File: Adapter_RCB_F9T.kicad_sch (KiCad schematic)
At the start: 48 parts, among them J1 USB_B_Micro, J2 Conn_01x04, J41 RCB_F9T, J51 Conn_Coaxial, J61 Conn_Coaxial, U11 XC6206PxxxMR, U21 LM27761, U31 CP2102-GMR-xQFN28, U51 BUF602xDBV, U61 BUF602xDBV

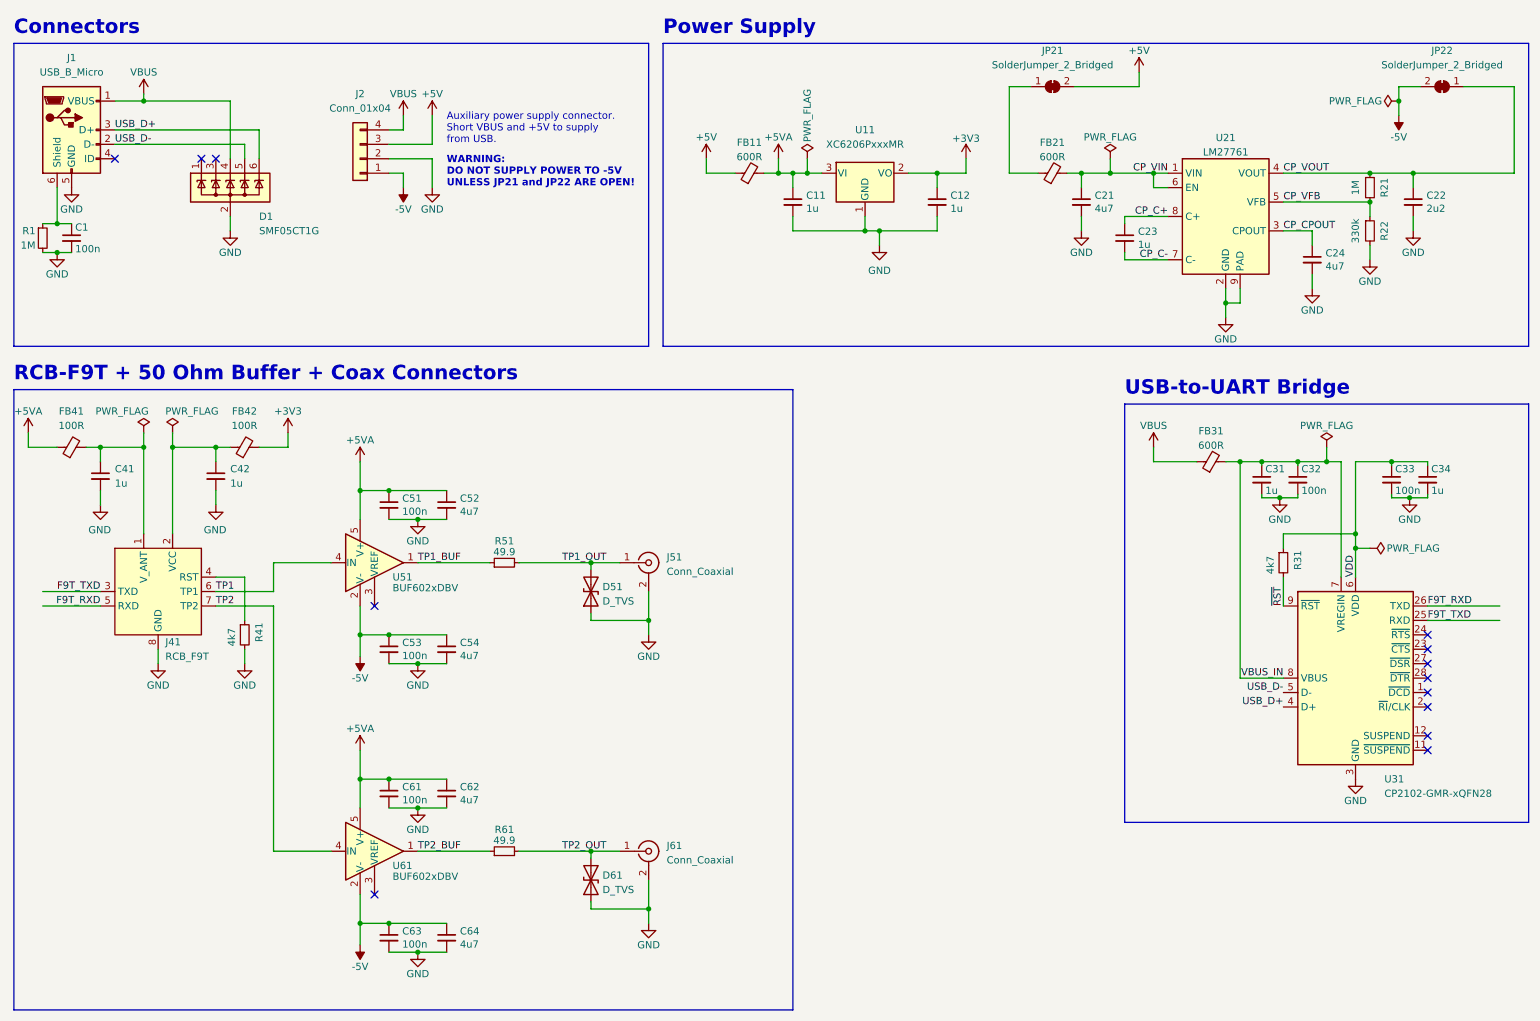
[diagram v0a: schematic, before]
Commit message: fix RCB-F9T NRST issue and move FB41 further away from mounting hole
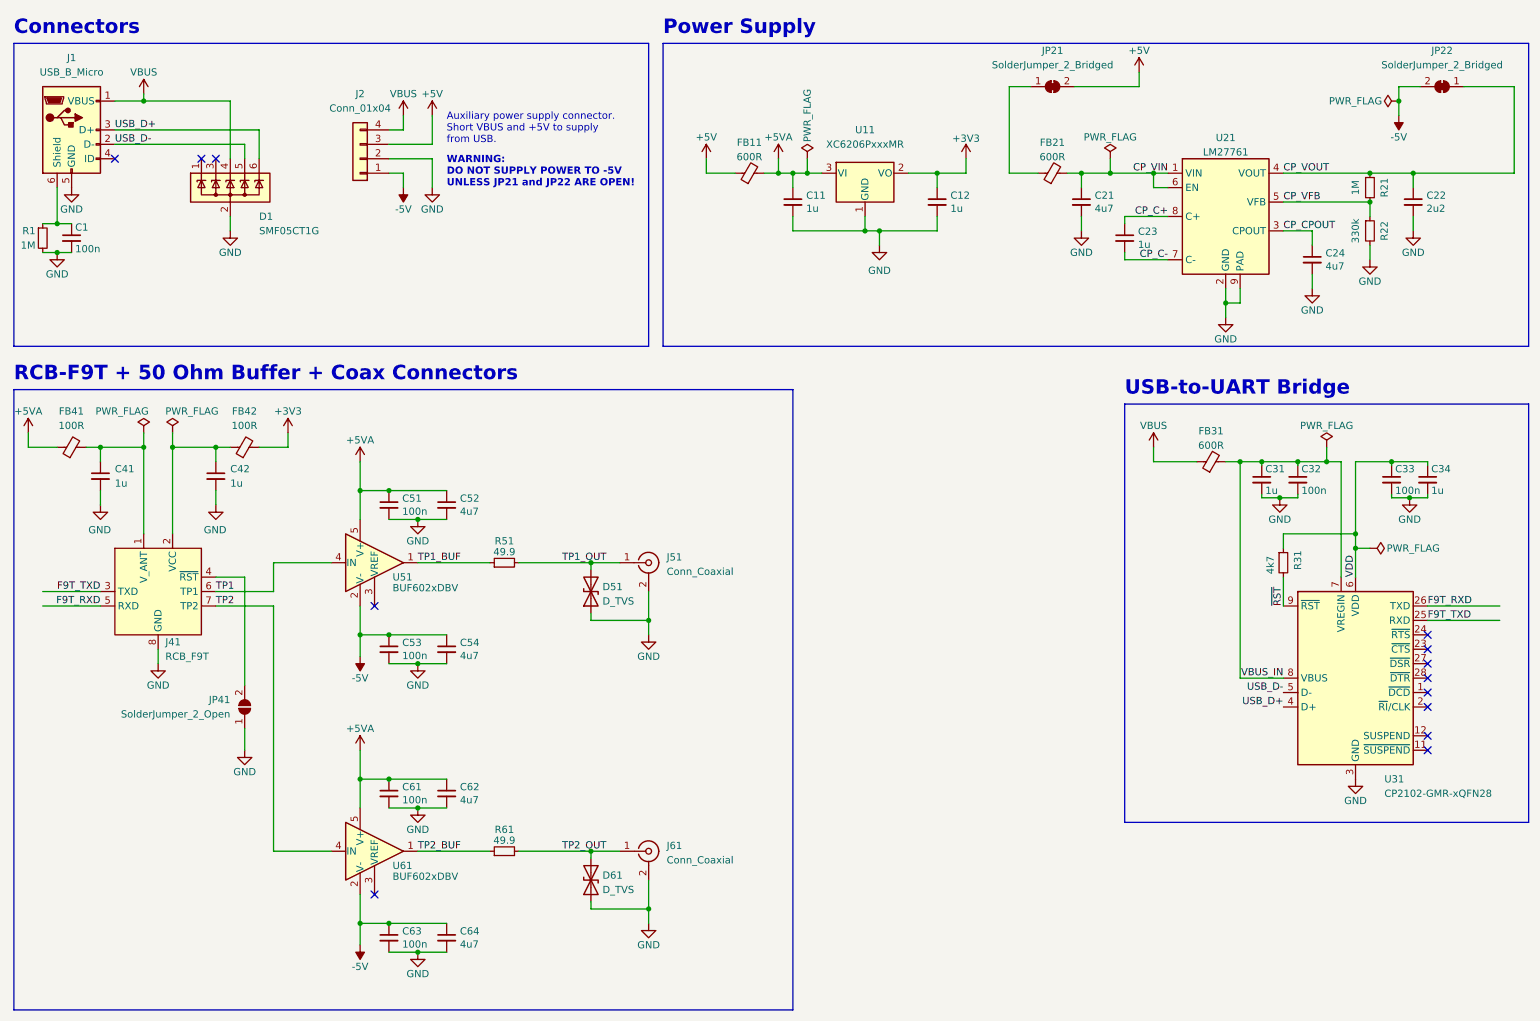
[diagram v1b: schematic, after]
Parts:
- removed R41: 4k7, Resistor_SMD:R_0402_1005Metric, symbol Device:R_Small
- added JP41: SolderJumper_2_Open, Jumper:SolderJumper-2_P1.3mm_Open_RoundedPad1.0x1.5mm, symbol Jumper:SolderJumper_2_Open
- J51, J61: MPN (none) -> 32K145-400L5; Manufacturer (none) -> Rosenberger
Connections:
- net GND: now also JP41.1 (A)
- net at J41.4 (~{RST}): now also JP41.2 (B)
